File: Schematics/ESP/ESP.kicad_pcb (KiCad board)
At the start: 2 copper layers, 180.5 x 111.7 mm, 82 parts, among them J1 Barrel_Jack, J11 Bumper 1, J12 Bumper 2, J14 Conn_02x19_Odd_Even, J15 UltraSconic B, J16 Conn_02x19_Odd_Even, J2 IMU, J3 Battery charger, J4 Motor A, J5 Motor B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

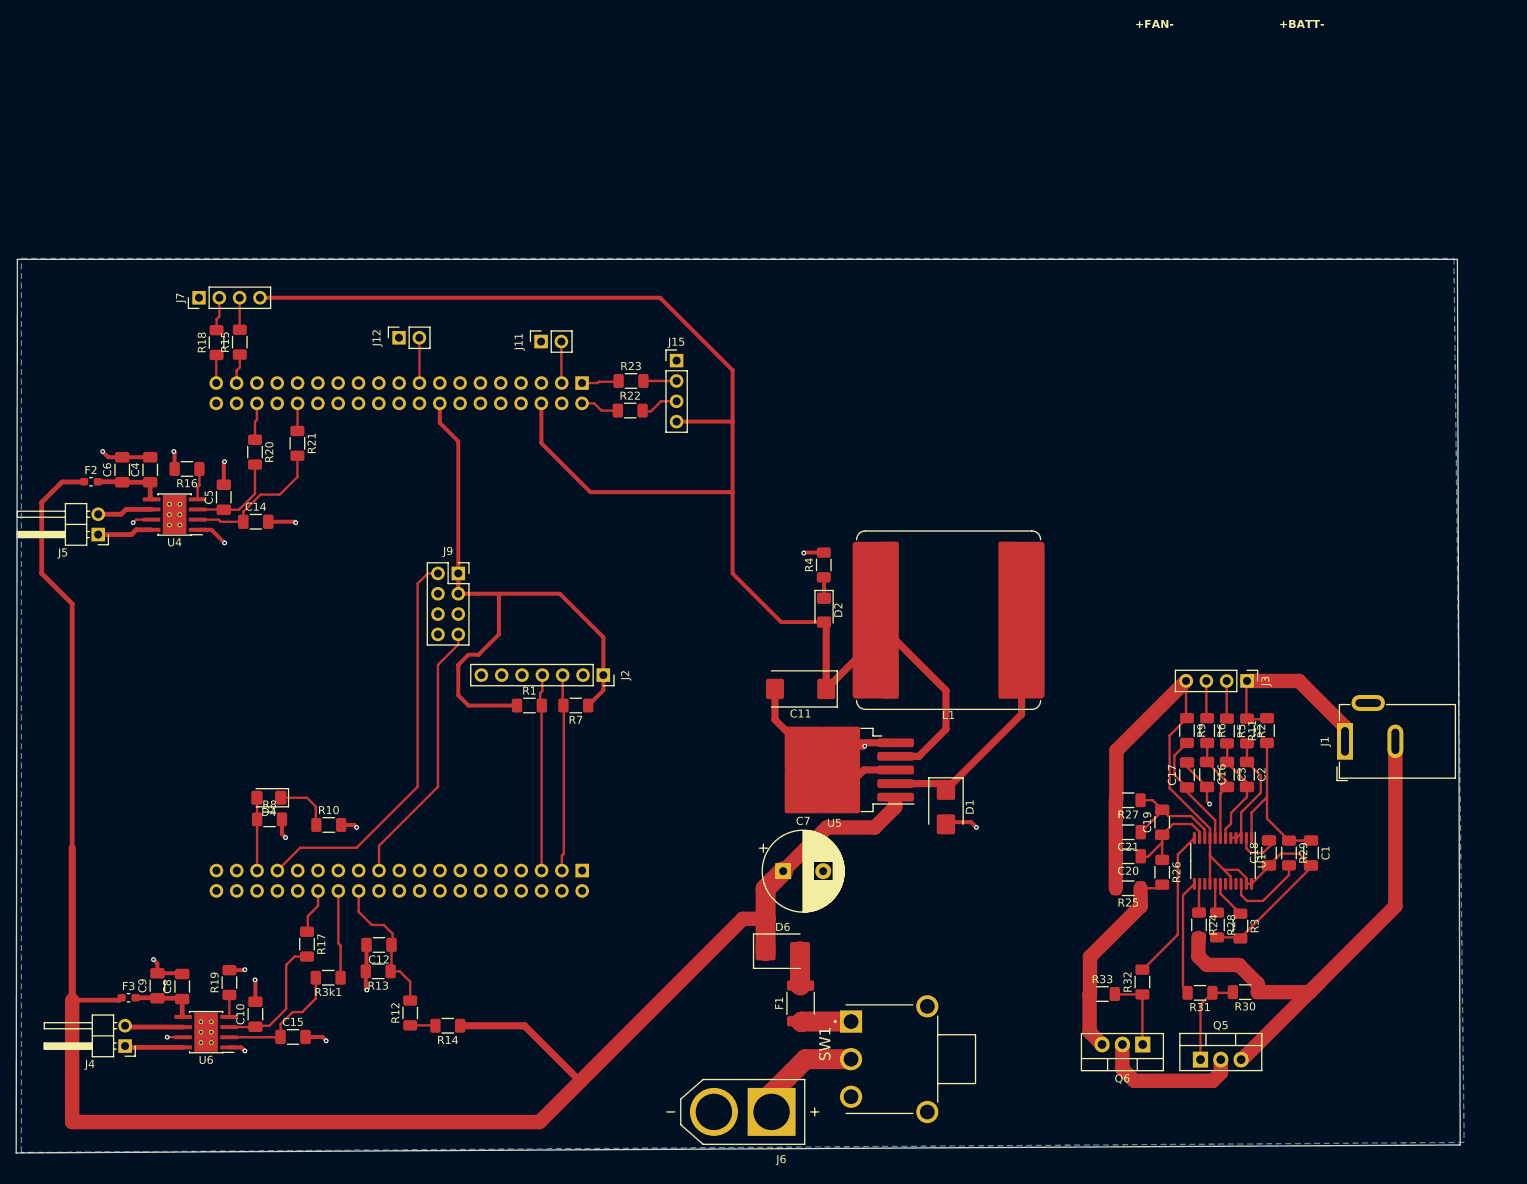
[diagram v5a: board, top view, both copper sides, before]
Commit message: fixed power tracks
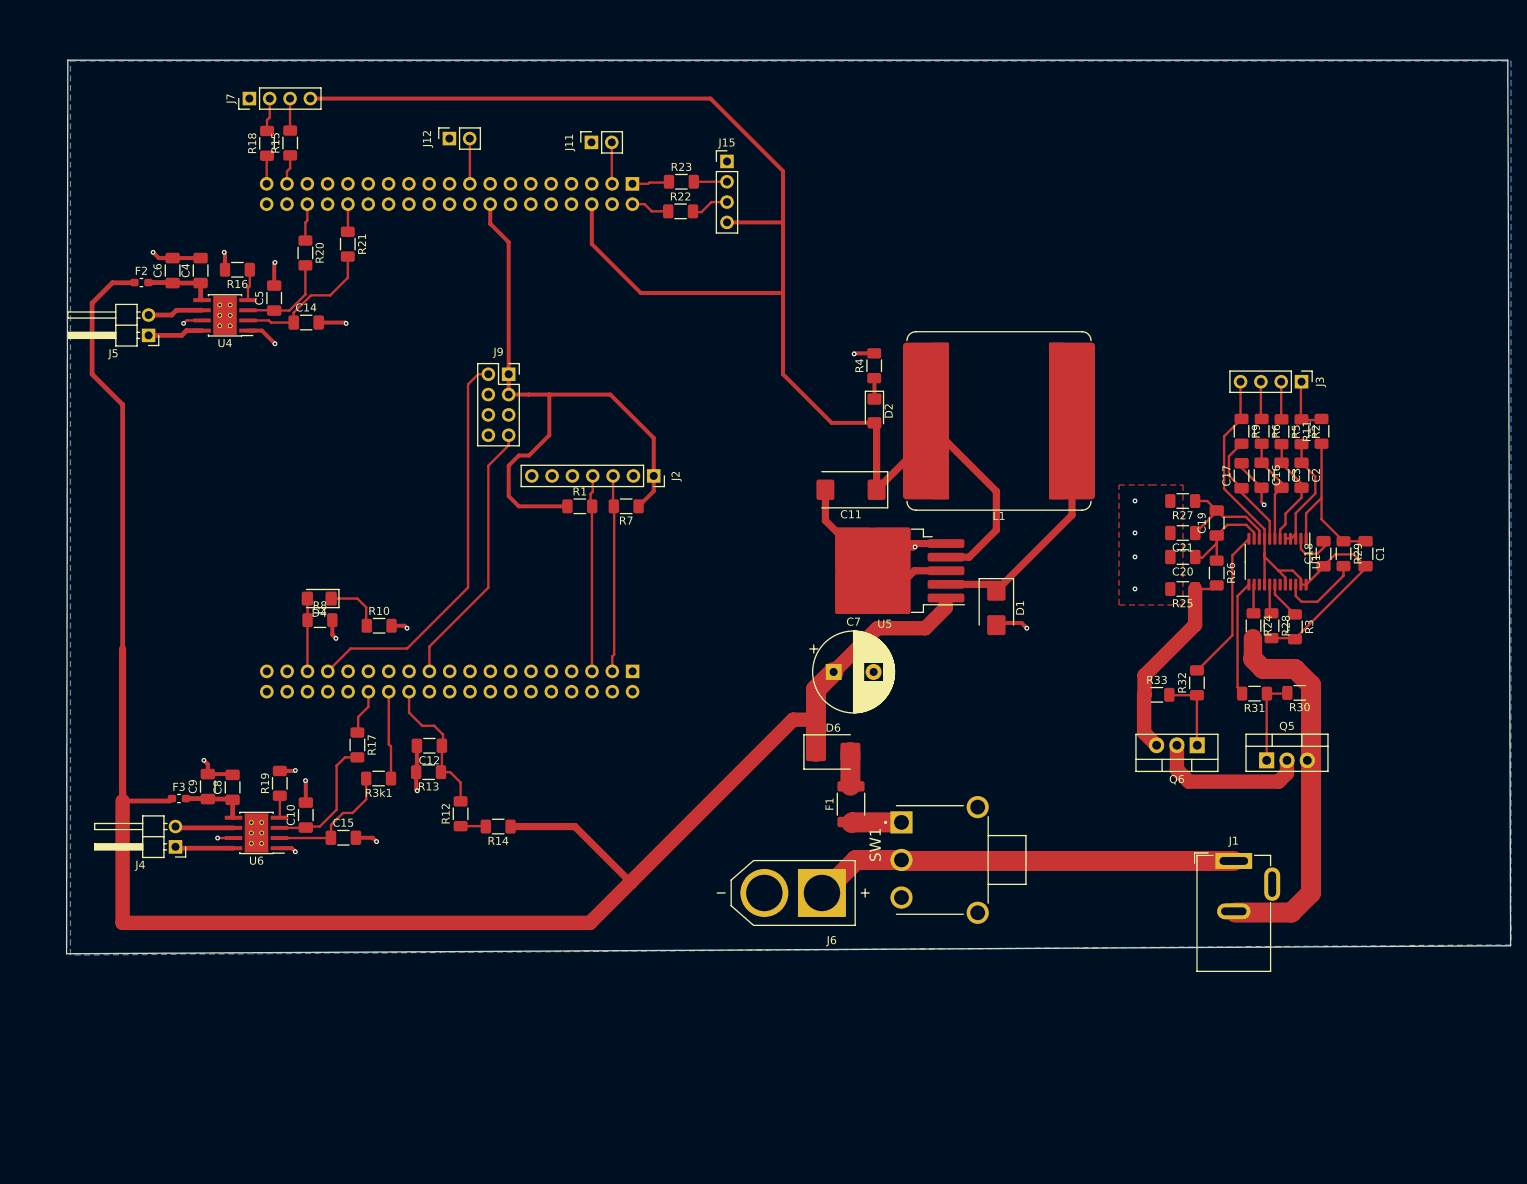
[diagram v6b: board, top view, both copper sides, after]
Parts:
- moved Q5 38.3 mm to (206.5, 122.4)
- moved R31 38.0 mm to (204.9, 114.1)
- moved C1 38.0 mm to (218.8, 96.6)
- moved C16 38.0 mm to (205.8, 86.8)
- moved C17 38.0 mm to (203.3, 86.8)
- moved C18 38.0 mm to (213.6, 96.6)
- moved C19 38.0 mm to (200.2, 92.8)
- moved C2 38.0 mm to (210.8, 86.8)
- moved C20 38.0 mm to (196.0, 97.0)
- moved C21 38.0 mm to (196.0, 94.0)
- moved C3 38.0 mm to (208.3, 86.8)
- moved J3 38.0 mm to (210.8, 75.1)
- moved Q6 38.0 mm to (197.8, 120.5)
- moved R11 38.0 mm to (213.3, 81.3)
- moved R2 38.0 mm to (210.8, 81.3)
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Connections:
- J1 pad 1: Cell3+ -> Battery+
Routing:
- net Battery+: track 14.0 -> 53.3 mm
- net Battery-: track 180.3 -> 150.8 mm, vias 19 -> 23
- net P-: track 67.5 -> 47.7 mm
- net Cell3+: track 22.8 -> 6.40 mm
- net Net-(Q5-D): track 18.0 -> 19.5 mm
- net Net-(Q5-G): track 11.2 -> 10.6 mm
- added copper zone on F.Cu, net Battery-
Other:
- outline, holes or cut-outs redrawn
- board text removed: "+BATT-"
- board text removed: "+FAN-"

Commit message: updated footprints
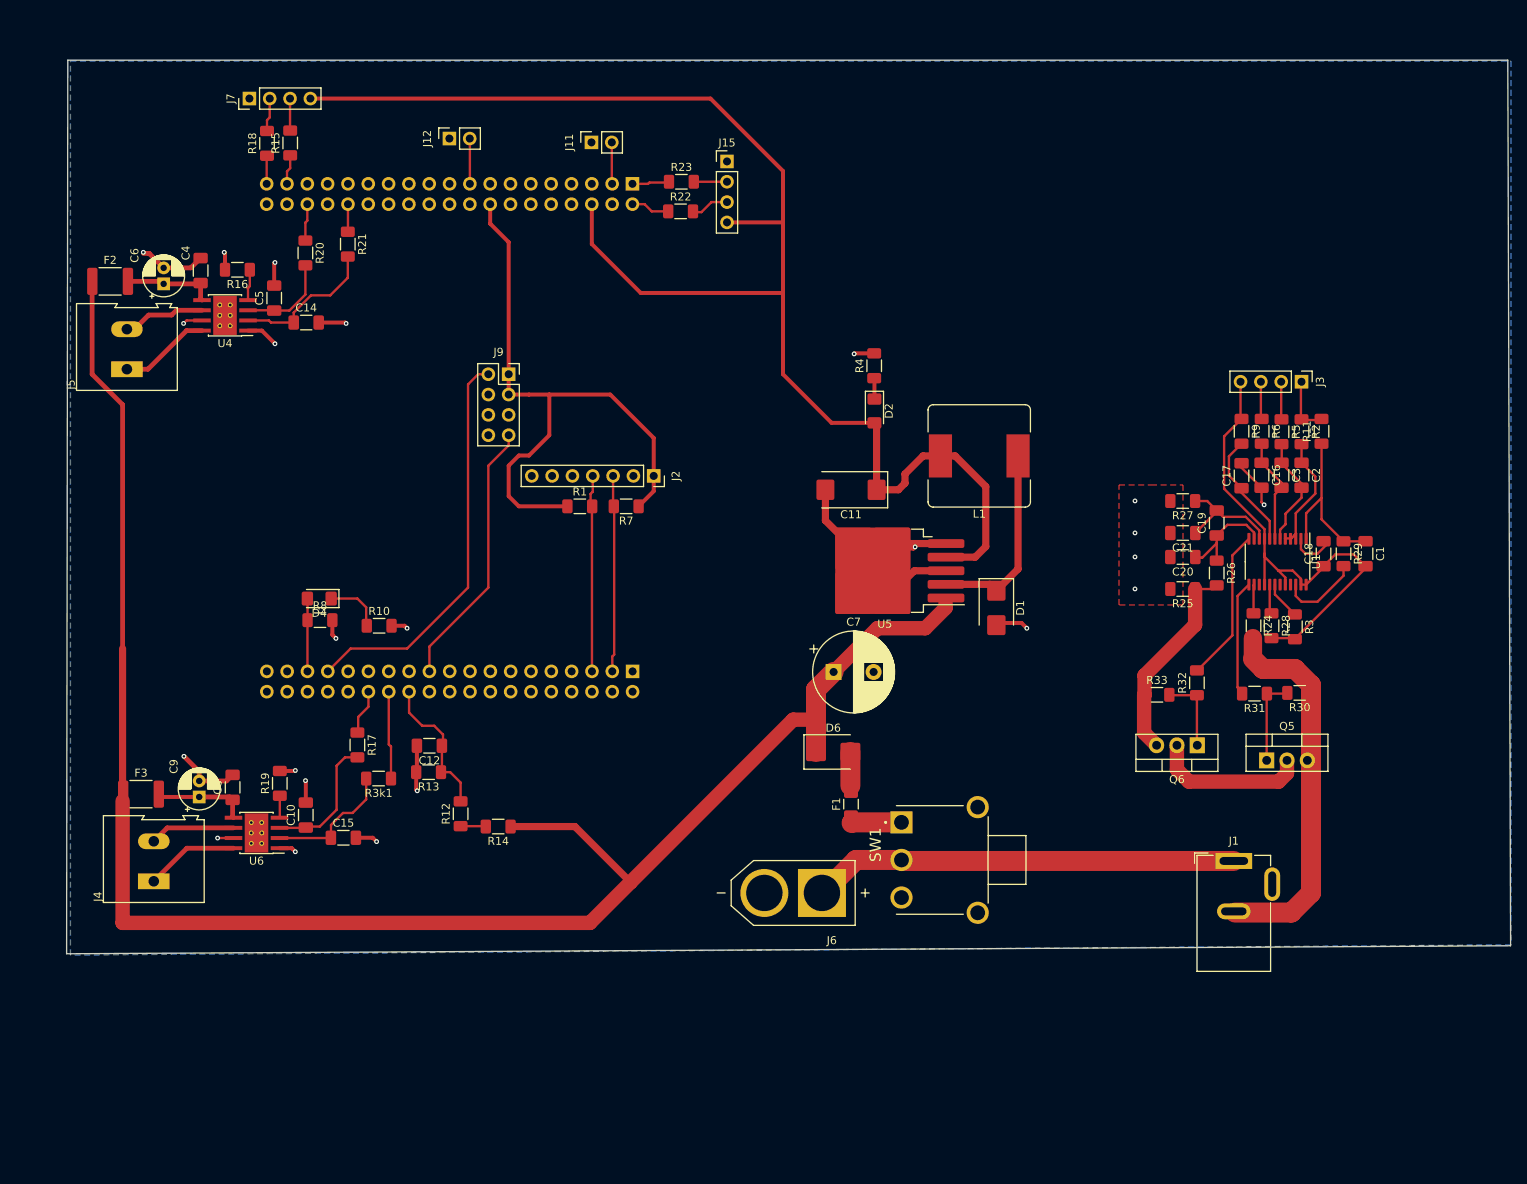
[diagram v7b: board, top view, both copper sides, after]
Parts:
- C6, C9: footprint Capacitor_SMD:C_1206_3216Metric_Pad1.33x1.80mm_HandSolder -> Capacitor_THT:CP_Radial_D5.0mm_P2.00mm
- F1: footprint Fuse:Fuse_1812_4532Metric_Pad1.30x3.40mm_HandSolder -> Fuse:Fuse_1206_3216Metric_Pad1.42x1.75mm_HandSolder
- F2, F3: footprint Fuse:Fuse_0603_1608Metric_Pad1.05x0.95mm_HandSolder -> Fuse:Fuse_1812_4532Metric_Pad1.30x3.40mm_HandSolder
- J4, J5: footprint Connector_PinHeader_2.54mm:PinHeader_1x02_P2.54mm_Horizontal -> TerminalBlock:TerminalBlock_Altech_AK300-2_P5.00mm
- L1: footprint Inductor_SMD:L_Bourns_SRP2313AA -> Inductor_SMD:L_Bourns_SRR1260
- moved J4 5.09 mm to (67.3, 137.5), turned to 90 degrees
- moved J5 5.02 mm to (64.0, 73.5), turned to 90 degrees
- moved L1 5.02 mm to (170.5, 84.4)
- moved F3 4.78 mm to (65.8, 126.7)
- moved F2 3.91 mm to (61.9, 62.5)
- moved C6 2.01 mm to (68.6, 62.9)
- moved C9 1.69 mm to (73.0, 127.0)
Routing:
- net +12V: track 235.6 -> 225.7 mm
- net Net-(D1-K): track 31.8 -> 24.6 mm
- net Battery-: track 150.8 -> 156.4 mm
- net +5V: track 184.9 -> 179.9 mm
- net MotorA-: track 7.08 -> 11.7 mm
- net MotorB-: track 6.92 -> 11.4 mm
- net Net-(U6-VM): track 7.94 -> 12.1 mm
- net MotorA+: track 7.08 -> 10.7 mm
- net MotorB+: track 6.92 -> 10.4 mm
- net Net-(U4-VM): track 8.67 -> 11.5 mm

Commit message: PCB and Schematics update for future usage
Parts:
- R1, R7: value 2k -> 10k
- moved R7 66.4 mm to (76.2, 47.2), turned to 0 degrees
- moved R1 47.4 mm to (131.6, 44.6), turned to -90 degrees
- moved R21 5.00 mm to (96.6, 58.1)
- moved J9 1.48 mm to (110.2, 74.1)
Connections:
- J14 pad 26: unconnected-(J14-Pin_26-Pad26) -> InputB2
- J14 pad 30: InputB2 -> unconnected-(J14-Pin_30-Pad30)
- J9 pad 2: RX -> TX
- J9 pad 3: +3.3V -> unconnected-(J9-Pin_3-Pad3)
- J9 pad 5: unconnected-(J9-Pin_5-Pad5) -> +3.3V
- J9 pad 7: TX -> RX
- R1 pad 1: +3.3V -> Battery-
- R1 pad 2: Net-(J16-Pin_5) -> Echo B
- R7 pad 1: +3.3V -> Battery-
- R7 pad 2: Net-(J16-Pin_3) -> Echo A
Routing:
- net TX: track 33.6 -> 64.0 mm
- net +3.3V: track 77.9 -> 55.9 mm
- net Battery-: track 156.4 -> 165.4 mm, vias 23 -> 26
- net RX: track 50.3 -> 42.5 mm
- net Echo B: track 4.54 -> 8.55 mm
- net Echo A: track 3.47 -> 7.32 mm
- net Net-(U4-IN2): track 18.3 -> 21.6 mm
